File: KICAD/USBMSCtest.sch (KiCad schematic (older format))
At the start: 15 parts, among them CN1 CN-ICSP, CN2 AE-FT234X, P1 CN_USB_A, U1 LM2931AZ-3.3_5.0, U2 PIC24FJ64GB002, Y1 Resonator_Small

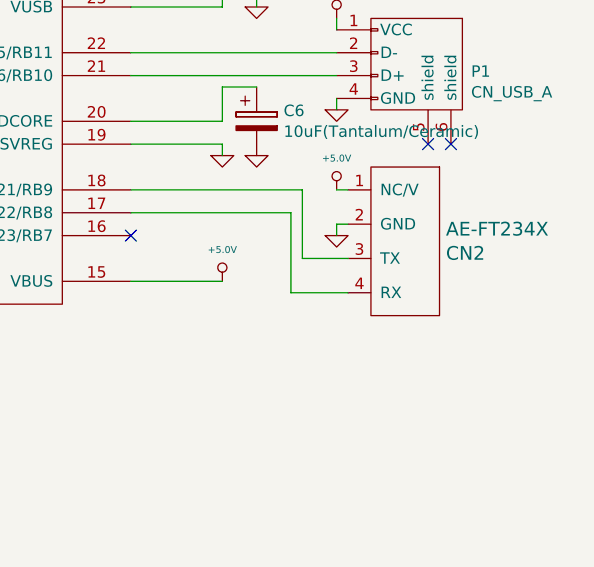
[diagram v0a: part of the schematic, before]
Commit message: UART pin RX-TX changed
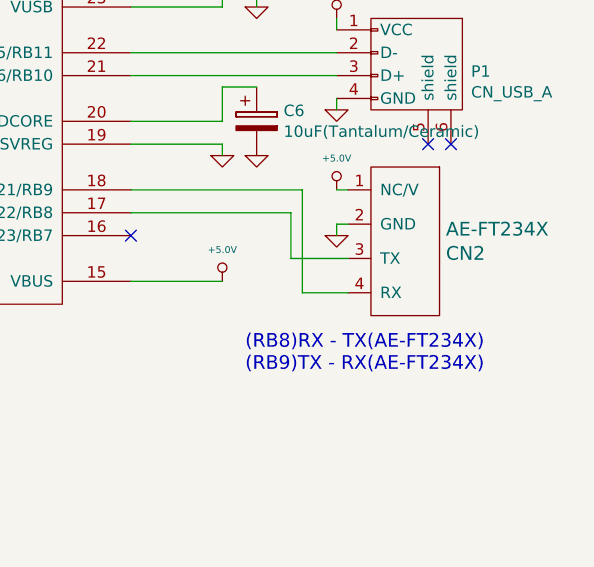
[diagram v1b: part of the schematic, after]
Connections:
- net at U2.17 (TCK/USBOEN/SCL1/RP8/PMD4/CN22/RB8): now also CN2.3 (TX); no longer CN2.4 (RX)
- net at U2.18 (TDO/SDA1/RP9/PMD3/RCV/CN21/RB9): now also CN2.4 (RX); no longer CN2.3 (TX)
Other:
- note added: "(RB8)RX - TX(AE-FT234X)\n(RB9)TX - RX(AE-FT234X)"
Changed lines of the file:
@@
 	7950 4750 8700 4750
-Wire Wire Line
-	8700 4750 8700 5050
-Wire Wire Line
-	8700 5050 8900 5050
-Wire Wire Line
-	8900 5200 8650 5200
-Wire Wire Line
-	8650 5200 8650 4850
 Wire Wire Line
 	8650 4850 7950 4850
@@
 NoConn ~ 9250 4550
 NoConn ~ 9350 4550
+Wire Wire Line
+	8700 5200 8900 5200
+Wire Wire Line
+	8700 4750 8700 5200
+Wire Wire Line
+	8650 4850 8650 5050
+Wire Wire Line
+	8650 5050 8900 5050
+Text Notes 8450 5550 0    60   ~ 0
+(RB8)RX - TX(AE-FT234X)\n(RB9)TX - RX(AE-FT234X)
 $EndSCHEMATC
